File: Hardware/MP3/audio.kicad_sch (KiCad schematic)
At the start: 25 parts, among them IC2 AK4493SEQ, U2 OPA1622IDRCR, Y1 ABM8-22.5792MHZ-D2Y-T

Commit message: feat: Made some changes to the DAC. Explicitly using register control (using I2C) with PCM audio. Planning to use 5.2V buck on 5V line, then Low noise LDO VREF for DAC, another for AMP power, and a 3v3 low noise LDO for DAC too.
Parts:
- C11, C13, C14, C16, C17, C18, C25, C27, C28, C29, C9: footprint (none) -> Capacitor_SMD:C_0603_1608Metric
- IC2: footprint QFP50P900X900X160-48N -> iclr:QFP50P900X900X160-48N
- U2: footprint DRC0010J -> iclr:DRC0010J
- Y1: footprint ABM810000MHZ12D2W -> iclr:ABM810000MHZ12D2W
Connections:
- net CS is gone; now on net GND: IC2.7 (SMUTE/CSN)
- net WCK is gone; now on net GND: IC2.6 (SSLOW/WCK)
- net CLOCK: now also IC2.46 (MCLK)
- net GND: now also IC2.12 (DIF2/CAD0), IC2.15 (DEM0), IC2.17 (ACKS/CAD1)
- net I2C: now reaches IC2.14 (I2C/INV)
- no-connect marks 0 -> 2
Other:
- note added: "Double check the pins, and add decoupling caps used for MCLK rather than DSP Pins 1 and 3 are interchangable? so it seems Can't use this...."
- note removed: "Double check the pins, and add decoupling caps used for MCLK rather than DSP Pins 1 and 3 are interchangable? so it seems"
- moved on the sheet: Y1

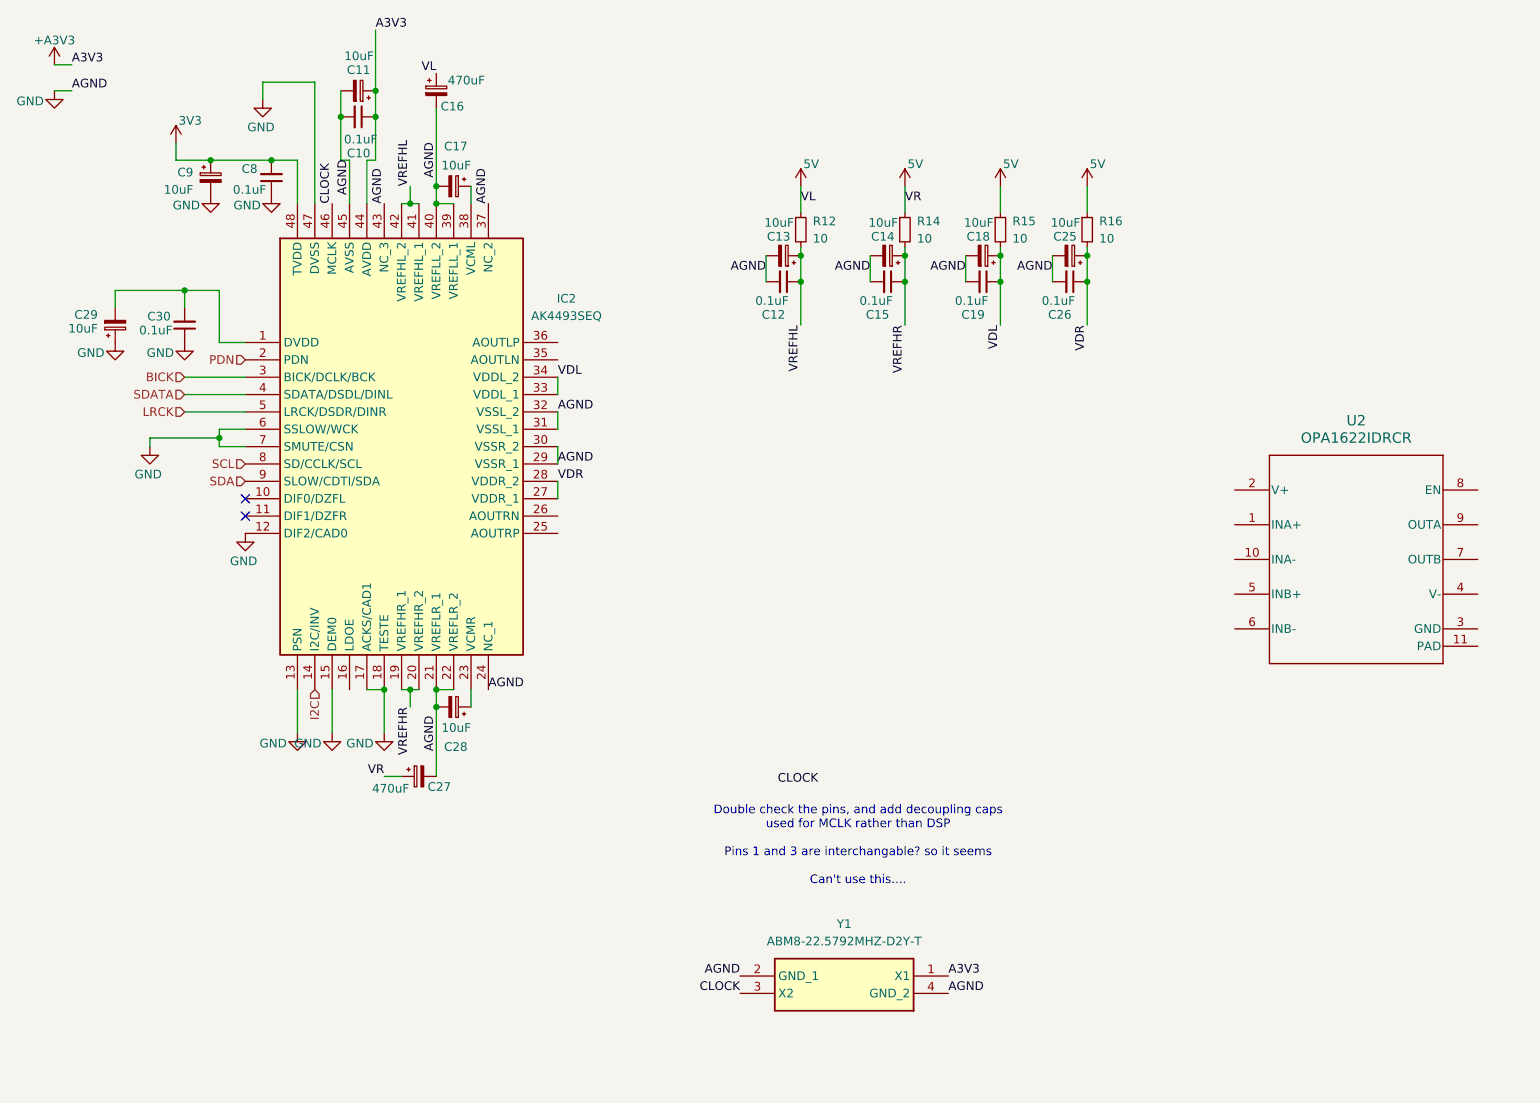
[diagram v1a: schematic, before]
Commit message: feat: Large progress made on the power system. Next steps, find oscillator, sort out LDO footprints, add OLED connectors and encoder connector.
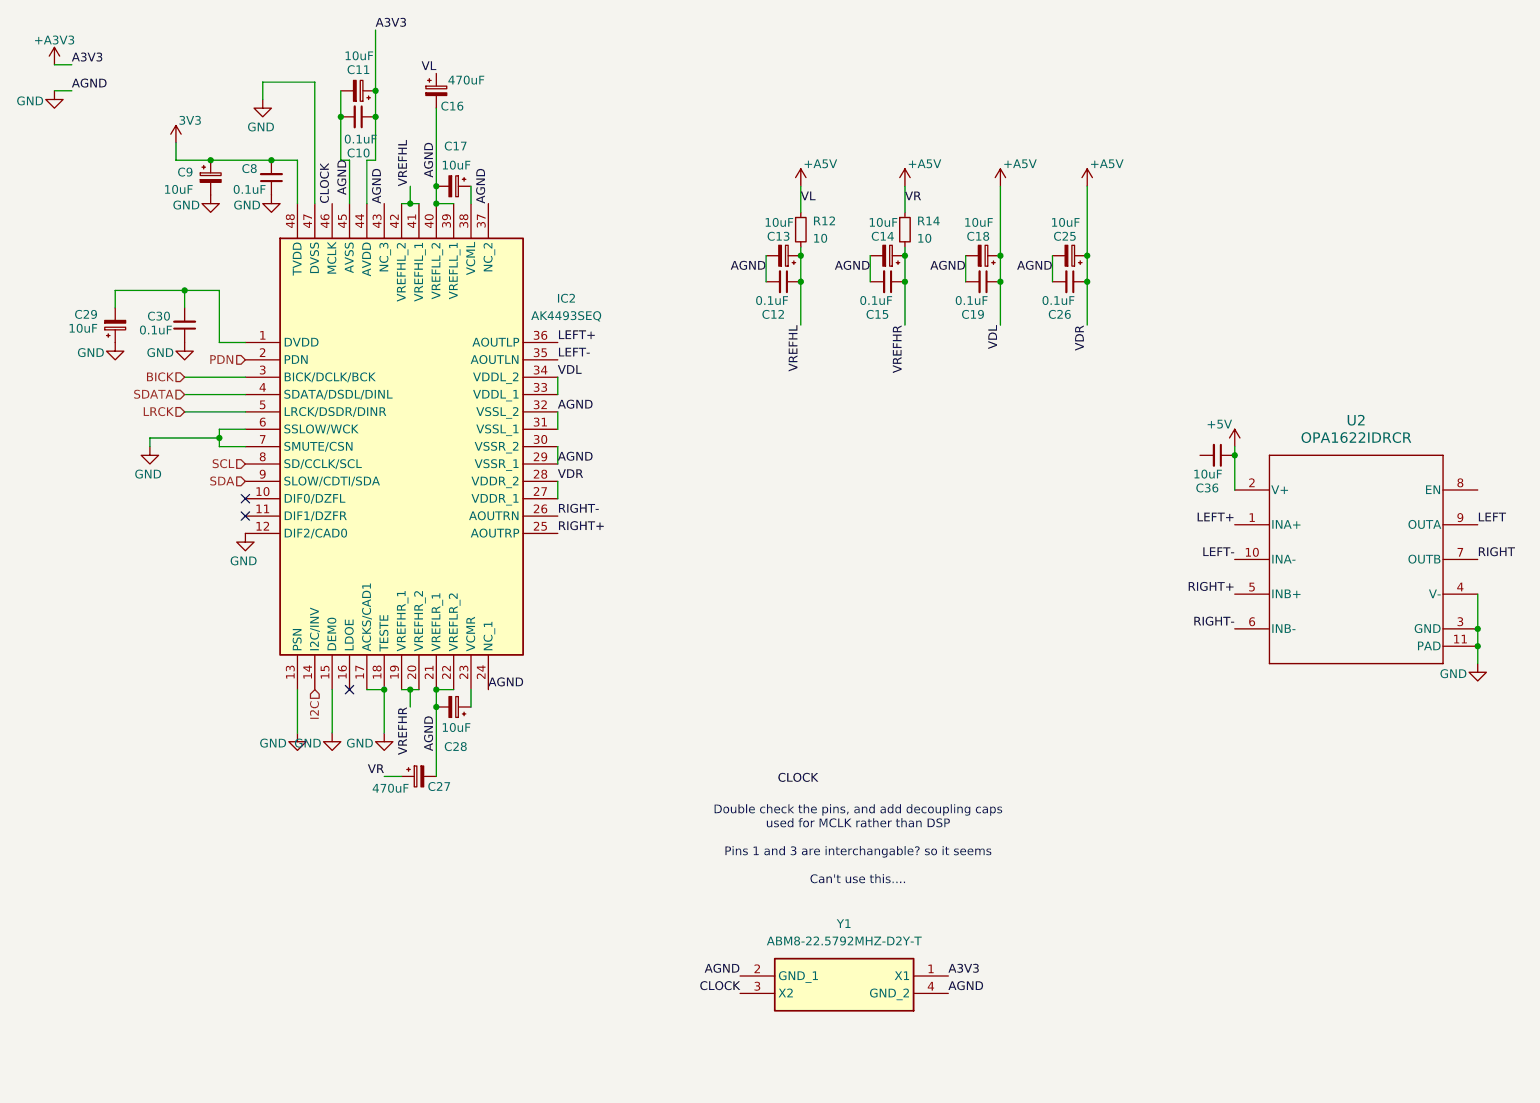
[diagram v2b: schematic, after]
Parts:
- removed R15, R16: 10, Resistor_SMD:R_0402_1005Metric, symbol Device:R_Small
- added C36: 10uF, Capacitor_SMD:C_0603_1608Metric, symbol Device:C_Small
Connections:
- net VDL is gone; now on net +A5V: C18.1, C19.1, IC2.33 (VDDL_1), IC2.34 (VDDL_2)
- net VDR is gone; now on net +A5V: C25.1, C26.1, IC2.27 (VDDR_1), IC2.28 (VDDR_2)
- net GND: now also U2.11 (PAD), U2.3 (GND), U2.4 (V-)
- net LEFT+: now reaches U2.1 (INA+)
- net LEFT+: now also IC2.36 (AOUTLP)
- net LEFT-: now reaches U2.10 (INA-)
- net LEFT-: now also IC2.35 (AOUTLN)
- net +5V: now reaches U2.2 (V+)
- net +5V: now also C36.1
- net RIGHT+: now reaches U2.5 (INB+)
- net RIGHT+: now also IC2.25 (AOUTRP)
- net RIGHT-: now reaches U2.6 (INB-)
- net RIGHT-: now also IC2.26 (AOUTRN)
- net RIGHT: now reaches U2.7 (OUTB)
- net LEFT: now reaches U2.9 (OUTA)
- net 5V renamed +A5V
- no-connect marks 2 -> 3
